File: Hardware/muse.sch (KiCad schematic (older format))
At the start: 47 parts, among them P1 3.5mm_line, P2 3.5mm_line, P3 RCA, P4 RCA, P5 ATX_PWR_OK, P6 ATX_PWR_OK, P7 ATX_PWR_OK, P8 ATX_PS_ON, P9 LED_Signal, Q1 FQP30N06L, Q2 FQP30N06L, Q3 FQP30N06L, Q4 FQP30N06L, Q5 FQP30N06L, Q6 FQP30N06L, SW1 PWR_SW, U1 MSGEQ7, U2 MSGEQ7, U3 74LS595, U4 Spark_Core

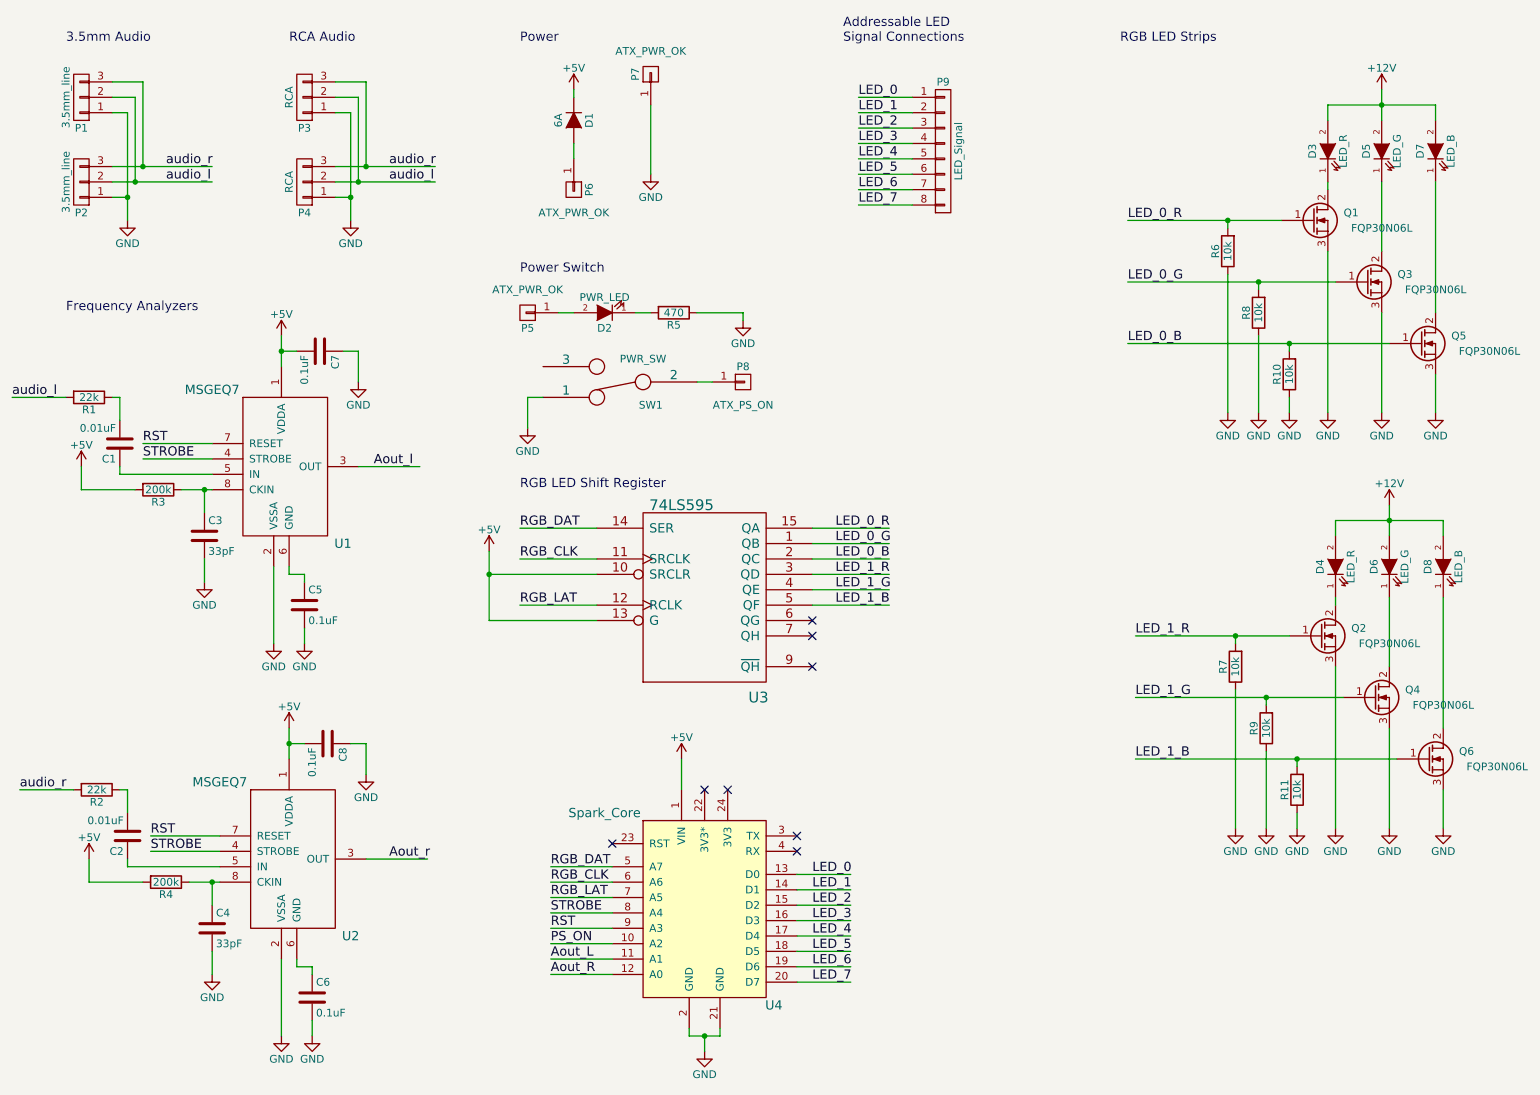
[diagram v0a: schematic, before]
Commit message: Preliminary PCB Layout in progress
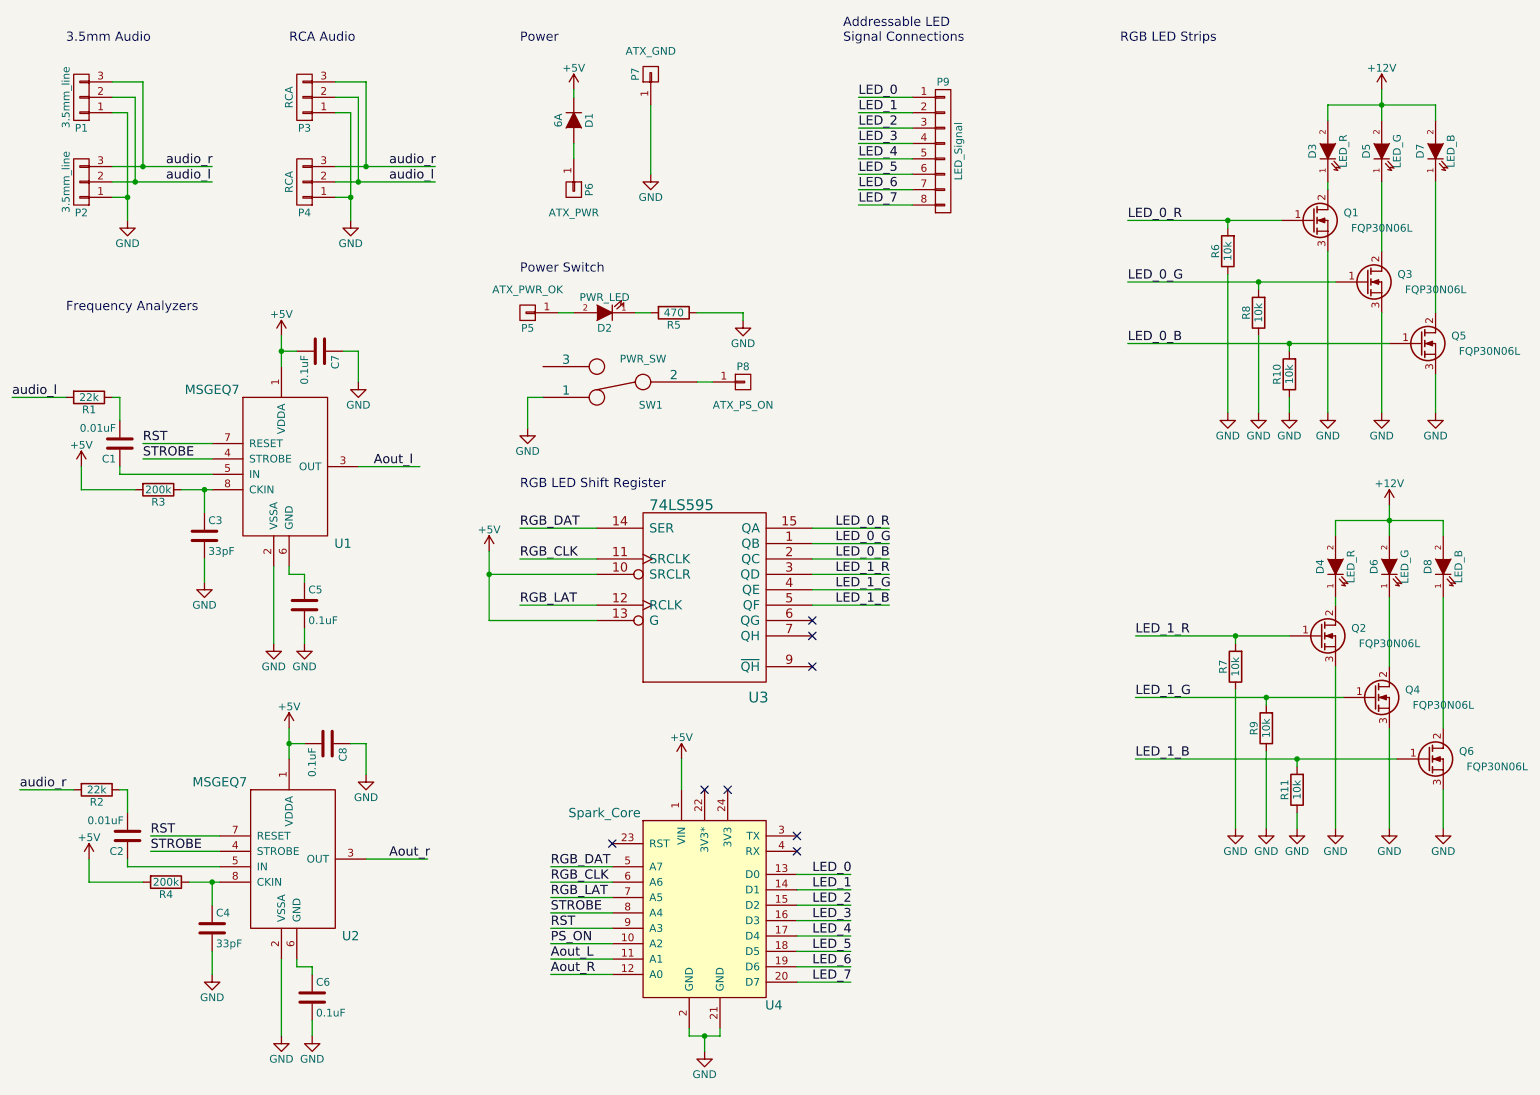
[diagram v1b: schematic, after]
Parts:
- C1, C2, C3, C4, C5, C6, C7, C8: footprint (none) -> Capacitors_ThroughHole:C_Rect_L7_W2_P5
- D1: footprint (none) -> Diodes_ThroughHole:Diode_DO-41_SOD81_Horizontal_RM10
- D2: footprint (none) -> LEDs:LED-3MM
- D3, D4, D5, D6, D7, D8, P5, P8: footprint (none) -> Pin_Headers:Pin_Header_Straight_1x01
- P1, P2: footprint (none) -> Pin_Headers:Pin_Header_Straight_1x03
- P3, P4: footprint (none) -> Pin_Headers:Audio_RCA_Vertical
- P6: value ATX_PWR_OK -> ATX_PWR; footprint (none) -> Pin_Headers:Pin_Header_Straight_1x01
- P7: value ATX_PWR_OK -> ATX_GND; footprint (none) -> Pin_Headers:Pin_Header_Straight_1x01
- P9: footprint (none) -> Pin_Headers:Pin_Header_Straight_1x08
- Q1, Q2, Q3, Q4, Q5, Q6: footprint (none) -> Transistors_TO-220:TO-220_Neutral123_Horizontal_LargePads
- R1, R10, R11, R2, R3, R4, R5, R6, R7, R8, R9: footprint (none) -> Resistors_ThroughHole:Resistor_Horizontal_RM10mm
- SW1: footprint (none) -> Pin_Headers:Pin_Header_Straight_1x02
- U1, U2: footprint (none) -> Housings_DIP:DIP-8_W7.62mm_LongPads
- U3: footprint (none) -> Housings_SSOP:SSOP-16_5.3x6.2mm_Pitch0.65mm
- U4: footprint (none) -> Pin_Headers:Spark_Core
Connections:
- wire segments 173 -> 151

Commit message: Preliminary board layout  complete
TODO: Route circuitry
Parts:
- Q1, Q2, Q3, Q4, Q5, Q6: footprint Transistors_TO-220:TO-220_Neutral123_Horizontal_LargePads -> Transistors_TO-220:TO-220_Neutral123_Vertical_LargePads
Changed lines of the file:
@@
 F 0 "Q3" H 9800 2350 50  0000 R CNN
 F 1 "FQP30N06L" H 10150 2250 50  0000 R CNN
-F 2 "Transistors_TO-220:TO-220_Neutral123_Horizontal_LargePads" H 9700 2400 29  0001 C CNN
+F 2 "Transistors_TO-220:TO-220_Neutral123_Vertical_LargePads" H 9700 2400 29  0001 C CNN
 F 3 "" H 9500 2300 60  0000 C CNN
 	1    9500 2300
@@
 F 0 "Q1" H 9450 1950 50  0000 R CNN
 F 1 "FQP30N06L" H 9800 1850 50  0000 R CNN
-F 2 "Transistors_TO-220:TO-220_Neutral123_Horizontal_LargePads" H 9350 2000 29  0001 C CNN
+F 2 "Transistors_TO-220:TO-220_Neutral123_Vertical_LargePads" H 9350 2000 29  0001 C CNN
 F 3 "" H 9150 1900 60  0000 C CNN
 	1    9150 1900
@@
 F 0 "Q5" H 10150 2750 50  0000 R CNN
 F 1 "FQP30N06L" H 10500 2650 50  0000 R CNN
-F 2 "Transistors_TO-220:TO-220_Neutral123_Horizontal_LargePads" H 10050 2800 29  0001 C CNN
+F 2 "Transistors_TO-220:TO-220_Neutral123_Vertical_LargePads" H 10050 2800 29  0001 C CNN
 F 3 "" H 9850 2700 60  0000 C CNN
 	1    9850 2700
@@
 F 0 "Q4" H 9850 5050 50  0000 R CNN
 F 1 "FQP30N06L" H 10200 4950 50  0000 R CNN
-F 2 "Transistors_TO-220:TO-220_Neutral123_Horizontal_LargePads" H 9750 5100 29  0001 C CNN
+F 2 "Transistors_TO-220:TO-220_Neutral123_Vertical_LargePads" H 9750 5100 29  0001 C CNN
 F 3 "" H 9550 5000 60  0000 C CNN
 	1    9550 5000
@@
 F 0 "Q2" H 9500 4650 50  0000 R CNN
 F 1 "FQP30N06L" H 9850 4550 50  0000 R CNN
-F 2 "Transistors_TO-220:TO-220_Neutral123_Horizontal_LargePads" H 9400 4700 29  0001 C CNN
+F 2 "Transistors_TO-220:TO-220_Neutral123_Vertical_LargePads" H 9400 4700 29  0001 C CNN
 F 3 "" H 9200 4600 60  0000 C CNN
 	1    9200 4600
@@
 F 0 "Q6" H 10200 5450 50  0000 R CNN
 F 1 "FQP30N06L" H 10550 5350 50  0000 R CNN
-F 2 "Transistors_TO-220:TO-220_Neutral123_Horizontal_LargePads" H 10100 5500 29  0001 C CNN
+F 2 "Transistors_TO-220:TO-220_Neutral123_Vertical_LargePads" H 10100 5500 29  0001 C CNN
 F 3 "" H 9900 5400 60  0000 C CNN
 	1    9900 5400
